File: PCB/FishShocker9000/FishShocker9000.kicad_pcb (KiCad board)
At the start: 2 copper layers, 133 parts, among them J1 Barrel_Jack, J10 P70-1000045R, J11 P70-1000045R, J12 P70-1000045R, J13 P70-1000045R, J14 P70-1000045R, J15 P70-1000045R, J16 P70-1000045R, J17 P70-1000045R, J18 P70-1000045R, J19 P70-1000045R, J20 P70-1000045R, J21 P70-1000045R, J22 P70-1000045R, J23 P70-1000045R, J24 P70-1000045R, J25 P70-1000045R, J26 P70-1000045R, J27 P70-1000045R, J28 P70-1000045R, J29 P70-1000045R, J3 P70-1000045R, J30 P70-1000045R, J31 P70-1000045R, J32 P70-1000045R, J33 P70-1000045R, J34 P70-1000045R, J35 P70-1000045R, J36 P70-1000045R, J37 P70-1000045R, J38 P70-1000045R, J39 P70-1000045R, J4 P70-1000045R, J40 P70-1000045R, J41 P70-1000045R, J42 P70-1000045R, J43 P70-1000045R, J44 P70-1000045R, J45 P70-1000045R, J46 P70-1000045R, J47 P70-1000045R, J48 P70-1000045R, J49 P70-1000045R, J5 P70-1000045R, J50 P70-1000045R, J51 P70-1000045R, J52 P70-1000045R, J53 P70-1000045R, J54 P70-1000045R, J55 P70-1000045R, J56 P70-1000045R, J57 P70-1000045R, J58 P70-1000045R, J59 P70-1000045R, J6 P70-1000045R, J60 P70-1000045R, J61 P70-1000045R, J62 P70-1000045R, J63 P70-1000045R, J64 P70-1000045R, J65 P70-1000045R, J66 P70-1000045R, J67 P70-1000045R, J68 P70-1000045R, J69 P70-1000045R, J7 P70-1000045R, J70 P70-1000045R, J71 P70-1000045R, J72 P70-1000045R, J73 P70-1000045R, J74 P70-1000045R, J8 P70-1000045R, J9 P70-1000045R, Q1 IRLZ44N, Q2 FQP27P06, U16 MP2331HGTL-Z, U19 DAC5311xDCK, U20 OPA197xD, U23 SN754410NE, U24 SN754410NE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

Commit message: Rerouted PCB layout to actually fit and work. Need to connect Pogo Pins
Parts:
- C8: footprint Capacitor_SMD:C_0201_0603Metric -> Capacitor_SMD:C_0603_1608Metric
- moved U23 7.50 mm to (319.4, 154.7)
- moved U24 7.50 mm to (319.4, 141.6)
- moved U25 7.50 mm to (319.4, 128.0)
- moved U26 7.50 mm to (319.4, 114.4)
- moved U29 7.50 mm to (319.4, 100.9)
- moved U30 7.50 mm to (319.4, 87.3)
- moved H4 6.52 mm to (271.5, 82.0)
- moved H1 5.52 mm to (405.5, 82.0)
- moved D10 4.03 mm to (356.1, 117.0)
- moved D11 4.03 mm to (356.0, 154.5)
- moved D12 4.03 mm to (393.0, 130.0)
- moved D13 4.03 mm to (374.6, 117.0)
- moved D2 4.03 mm to (374.5, 154.2)
- moved D3 4.03 mm to (393.1, 154.5)
- moved D4 4.03 mm to (355.9, 143.0)
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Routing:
- net BUCK_VOUT: track 68.2 -> 310.2 mm, vias 1 -> 2
- net GND: track 112.4 -> 225.7 mm, vias 16 -> 15
- net (no net): track 49.1 -> 0.00 mm
- net A11: track 152.2 -> 135.5 mm
- net Plate 5.1: track 43.9 -> 58.5 mm, vias 0 -> 1
- net Plate 9.1: track 72.5 -> 86.5 mm, vias 0 -> 1
- net Plate 12.2: track 86.9 -> 100.8 mm, vias 0 -> 1
- net Plate 3.1: track 29.6 -> 43.4 mm, vias 0 -> 1
- net Plate 1.1: track 17.4 -> 30.6 mm, vias 0 -> 1
- net Plate 9.2: track 65.4 -> 76.3 mm, vias 0 -> 1
- net Plate 7.1: track 61.2 -> 72.0 mm, vias 0 -> 1
- net Plate 5.2: track 36.8 -> 47.5 mm, vias 0 -> 1
- net Plate 12.1: track 79.8 -> 90.5 mm, vias 0 -> 1
- net Plate 3.2: track 22.5 -> 33.0 mm, vias 0 -> 1
- net Polarity Enable 2: track 214.9 -> 205.2 mm
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- added copper zone on B.Cu, net GND
- removed copper zone on F.Cu, net BUCK_VOUT
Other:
- board outline added: 140 x 285.9 mm
- board text removed: "LED ON = GOOD POWER"

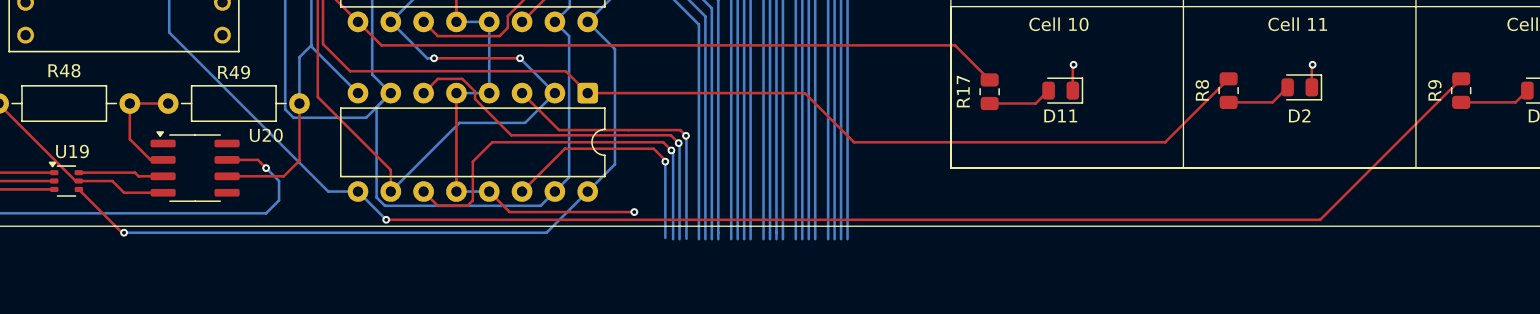
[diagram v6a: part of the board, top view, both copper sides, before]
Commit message: Fixed some other issues. Pogo Pins still not connected
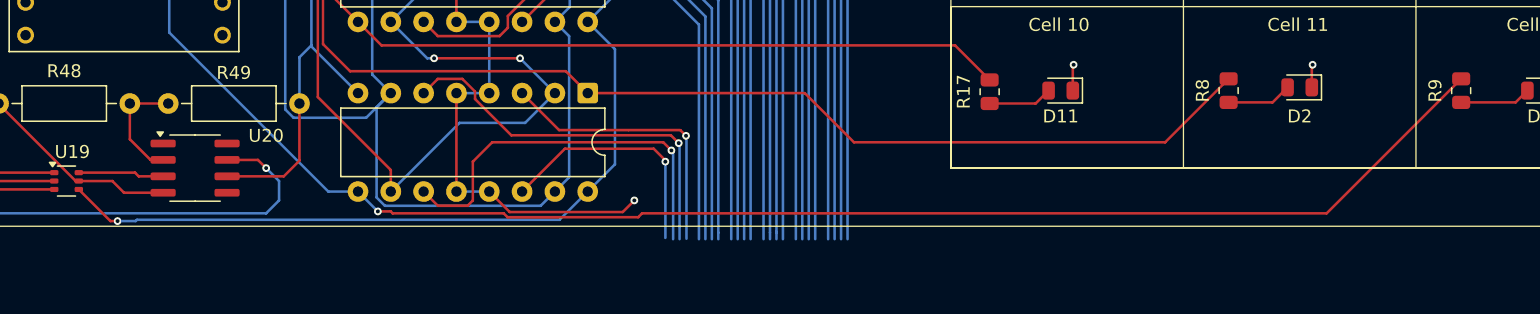
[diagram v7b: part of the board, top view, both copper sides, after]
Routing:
- net BUCK_VOUT: track 310.2 -> 309.4 mm
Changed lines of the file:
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@@
 	)
 	(segment
+		(start 282.45 164.6)
+		(end 280 162.15)
+		(width 0.2)
+		(layer "F.Cu")
+		(net 5)
+	)
+	(segment
 		(start 392.8625 96.8625)
 		(end 392 96)
@@
 	)
 	(segment
-		(start 283.5 165.5)
-		(end 283.35 165.5)
-		(width 0.2)
-		(layer "F.Cu")
-		(net 5)
-	)
-	(segment
 		(start 390.608198 107.5)
 		(end 388.5241 107.5)
@@
 	)
 	(segment
-		(start 387.0241 106)
-		(end 381.08294 106)
+		(start 283 164.6)
+		(end 282.45 164.6)
 		(width 0.2)
 		(layer "F.Cu")
@@
 	)
 	(segment
-		(start 382.9641 100.325)
-		(end 382.9641 103.17)
+		(start 387.0241 106)
+		(end 381.08294 106)
 		(width 0.2)
 		(layer "F.Cu")
@@
 	)
 	(segment
-		(start 283.35 165.5)
-		(end 280 162.15)
+		(start 382.9641 100.325)
+		(end 382.9641 103.17)
 		(width 0.2)
 		(layer "F.Cu")
@@
 	)
 	(via
-		(at 283.5 165.5)
+		(at 283 164.6)
 		(size 0.6)
 		(drill 0.3)
@@
 	)
 	(segment
+		(start 284.4 164.6)
+		(end 284.5 164.5)
+		(width 0.2)
+		(layer "B.Cu")
+		(net 5)
+	)
+	(segment
 		(start 321.5 110.608)
 		(end 321.5 119.949)
@@
 	)
 	(segment
+		(start 284.5 164.5)
+		(end 317.205 164.5)
+		(width 0.2)
+		(layer "B.Cu")
+		(net 5)
+	)
+	(segment
 		(start 285.28 91.79)
 		(end 278.93 98.14)
@@
 	)
 	(segment
+		(start 317.205 164.5)
+		(end 319.39 162.315)
+		(width 0.2)
+		(layer "B.Cu")
+		(net 5)
+	)
+	(segment
 		(start 319.39 162.315)
 		(end 321.5 160.205)
@@
 	)
 	(segment
-		(start 297.509 85.401)
-		(end 291.12 91.79)
+		(start 283 164.6)
+		(end 284.4 164.6)
 		(width 0.2)
 		(layer "B.Cu")
@@
 	)
 	(segment
-		(start 316.205 165.5)
-		(end 283.5 165.5)
+		(start 297.509 85.401)
+		(end 291.12 91.79)
 		(width 0.2)
 		(layer "B.Cu")
@@
 	)
 	(segment
-		(start 319.39 162.315)
-		(end 316.205 165.5)
-		(width 0.2)
-		(layer "B.Cu")
-		(net 5)
-	)
-	(segment
 		(start 321.5 147.071)
 		(end 319.39 149.181)
@@
 	)
 	(segment
-		(start 303.795 164.5)
-		(end 376.0875 164.5)
+		(start 304.1475 163.8525)
+		(end 304.295 164)
+		(width 0.2)
+		(layer "F.Cu")
+		(net 34)
+	)
+	(segment
+		(start 313.1889 164.301)
+		(end 323.3 164.301)
+		(width 0.2)
+		(layer "F.Cu")
+		(net 34)
+	)
+	(segment
+		(start 312.8879 164)
+		(end 313.1889 164.301)
+		(width 0.2)
+		(layer "F.Cu")
+		(net 34)
+	)
+	(segment
+		(start 323.601 164)
+		(end 376.5875 164)
+		(width 0.2)
+		(layer "F.Cu")
+		(net 34)
+	)
+	(segment
+		(start 304.295 164)
+		(end 312.8879 164)
 		(width 0.2)
 		(layer "F.Cu")
@@
 	)
 	(segment
-		(start 376.0875 164.5)
+		(start 376.5875 164)
 		(end 387 153.5875)
 		(width 0.2)
@@
 		(net 34)
 	)
+	(segment
+		(start 303.1475 163.8525)
+		(end 304.1475 163.8525)
+		(width 0.2)
+		(layer "F.Cu")
+		(net 34)
+	)
+	(segment
+		(start 323.3 164.301)
+		(end 323.601 164)
+		(width 0.2)
+		(layer "F.Cu")
+		(net 34)
+	)
 	(via
-		(at 303.795 164.5)
+		(at 303.1475 163.8525)
 		(size 0.6)
 		(drill 0.3)
@@
 	(segment
 		(start 301.61 162.315)
-		(end 303.795 164.5)
+		(end 303.1475 163.8525)
 		(width 0.2)
 		(layer "B.Cu")
@@
 	)
 	(segment
+		(start 313.355 163.9)
+		(end 311.77 162.315)
+		(width 0.2)
+		(layer "F.Cu")
+		(net 110)
+	)
+	(segment
 		(start 381.1 92.2)
 		(end 382.0841 92.2)
@@
 	)
 	(segment
+		(start 322.1 163.9)
+		(end 313.355 163.9)
+		(width 0.2)
+		(layer "F.Cu")
+		(net 110)
+	)
+	(segment
 		(start 309.23 141.561)
 		(end 309.23 149.181)
@@
 	)
 	(segment
-		(start 313.355 163.9)
-		(end 323 163.9)
+		(start 356.875 143)
+		(end 356.875 141.125)
 		(width 0.2)
 		(layer "F.Cu")
@@
 	)
 	(segment
-		(start 356.875 143)
-		(end 356.875 141.125)
+		(start 273.79 155.5)
+		(end 273.79 155.53487)
 		(width 0.2)
 		(layer "F.Cu")
@@
 	)
 	(segment
-		(start 273.79 155.5)
-		(end 273.79 155.53487)
+		(start 323 163)
+		(end 322.1 163.9)
 		(width 0.2)
 		(layer "F.Cu")
@@
 		(net 110)
 	)
-	(segment
-		(start 311.77 162.315)
-		(end 313.355 163.9)
-		(width 0.2)
-		(layer "F.Cu")
-		(net 110)
-	)
 	(via
 		(at 357 128)
@@
 	)
 	(via
-		(at 323 163.9)
+		(at 323 163)
 		(size 0.6)
 		(drill 0.3)

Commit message: Placed Pogo Pins
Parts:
- added J100: P70-1000045R, Library:HARWIN_P70-1000045R, F.Cu at (293.8, 347.6)
- added J101: P70-1000045R, Library:HARWIN_P70-1000045R, F.Cu at (309.7, 353.6)
- added J102: P70-1000045R, Library:HARWIN_P70-1000045R, F.Cu at (318.0, 250.9)
- added J103: P70-1000045R, Library:HARWIN_P70-1000045R, F.Cu at (310.1, 237.2)
- added J104: P70-1000045R, Library:HARWIN_P70-1000045R, F.Cu at (329.4, 286.1)
- added J105: P70-1000045R, Library:HARWIN_P70-1000045R, F.Cu at (345.3, 292.1)
- added J106: P70-1000045R, Library:HARWIN_P70-1000045R, F.Cu at (364.2, 278.3)
- added J107: P70-1000045R, Library:HARWIN_P70-1000045R, F.Cu at (380.6, 312.4)
- added J108: P70-1000045R, Library:HARWIN_P70-1000045R, F.Cu at (323.0, 329.9)
- added J109: P70-1000045R, Library:HARWIN_P70-1000045R, F.Cu at (309.7, 347.4)
- added J110: P70-1000045R, Library:HARWIN_P70-1000045R, F.Cu at (293.8, 224.7)
- added J111: P70-1000045R, Library:HARWIN_P70-1000045R, F.Cu at (285.3, 209.9)
- added J112: P70-1000045R, Library:HARWIN_P70-1000045R, F.Cu at (323.6, 213.8)
- added J113: P70-1000045R, Library:HARWIN_P70-1000045R, F.Cu at (315.9, 227.4)
- added J114: P70-1000045R, Library:HARWIN_P70-1000045R, F.Cu at (364.6, 271.2)
- added J115: P70-1000045R, Library:HARWIN_P70-1000045R, F.Cu at (381.5, 237.2)
- added J116: P70-1000045R, Library:HARWIN_P70-1000045R, F.Cu at (288.3, 275.3)
- added J117: P70-1000045R, Library:HARWIN_P70-1000045R, F.Cu at (285.3, 291.9)
- added J118: P70-1000045R, Library:HARWIN_P70-1000045R, F.Cu at (323.7, 295.8)
- added J119: P70-1000045R, Library:HARWIN_P70-1000045R, F.Cu at (345.7, 298.7)
- added J120: P70-1000045R, Library:HARWIN_P70-1000045R, F.Cu at (364.5, 319.2)
- added J121: P70-1000045R, Library:HARWIN_P70-1000045R, F.Cu at (381.3, 319.2)
- added J122: P70-1000045R, Library:HARWIN_P70-1000045R, F.Cu at (288.1, 193.3)
- added J123: P70-1000045R, Library:HARWIN_P70-1000045R, F.Cu at (280.4, 207.0)
- added J124: P70-1000045R, Library:HARWIN_P70-1000045R, F.Cu at (329.2, 244.9)
- added J125: P70-1000045R, Library:HARWIN_P70-1000045R, F.Cu at (345.2, 251.0)
- added J126: P70-1000045R, Library:HARWIN_P70-1000045R, F.Cu at (364.0, 237.1)
- added J127: P70-1000045R, Library:HARWIN_P70-1000045R, F.Cu at (356.5, 250.8)
- added J128: P70-1000045R, Library:HARWIN_P70-1000045R, F.Cu at (293.9, 312.5)
- added J129: P70-1000045R, Library:HARWIN_P70-1000045R, F.Cu at (309.7, 312.0)
- added J130: P70-1000045R, Library:HARWIN_P70-1000045R, F.Cu at (328.8, 298.8)
- added J131: P70-1000045R, Library:HARWIN_P70-1000045R, F.Cu at (315.8, 309.5)
- added J132: P70-1000045R, Library:HARWIN_P70-1000045R, F.Cu at (389.0, 333.0)
- added J133: P70-1000045R, Library:HARWIN_P70-1000045R, F.Cu at (351.3, 330.0)
- added J134: P70-1000045R, Library:HARWIN_P70-1000045R, F.Cu at (323.0, 207.1)
- added J135: P70-1000045R, Library:HARWIN_P70-1000045R, F.Cu at (309.8, 230.5)
- added J136: P70-1000045R, Library:HARWIN_P70-1000045R, F.Cu at (353.6, 230.3)
- added J137: P70-1000045R, Library:HARWIN_P70-1000045R, F.Cu at (345.1, 245.1)
- added J138: P70-1000045R, Library:HARWIN_P70-1000045R, F.Cu at (359.2, 234.5)
- added J139: P70-1000045R, Library:HARWIN_P70-1000045R, F.Cu at (351.4, 247.9)
- added J140: P70-1000045R, Library:HARWIN_P70-1000045R, F.Cu at (318.0, 291.9)
- added J141: P70-1000045R, Library:HARWIN_P70-1000045R, F.Cu at (310.2, 278.1)
- added J142: P70-1000045R, Library:HARWIN_P70-1000045R, F.Cu at (353.5, 312.3)
- added J143: P70-1000045R, Library:HARWIN_P70-1000045R, F.Cu at (320.9, 312.4)
- added J144: P70-1000045R, Library:HARWIN_P70-1000045R, F.Cu at (359.1, 316.2)
- added J145: P70-1000045R, Library:HARWIN_P70-1000045R, F.Cu at (356.4, 332.6)
- added J2: P70-1000045R, Library:HARWIN_P70-1000045R, F.Cu at (323.7, 172.9)
- added J75: P70-1000045R, Library:HARWIN_P70-1000045R, F.Cu at (316.0, 186.4)
- added J76: P70-1000045R, Library:HARWIN_P70-1000045R, F.Cu at (329.3, 204.0)
- added J77: P70-1000045R, Library:HARWIN_P70-1000045R, F.Cu at (320.8, 189.2)
- added J78: P70-1000045R, Library:HARWIN_P70-1000045R, F.Cu at (329.2, 210.0)
- added J79: P70-1000045R, Library:HARWIN_P70-1000045R, F.Cu at (345.1, 204.0)
- added J80: P70-1000045R, Library:HARWIN_P70-1000045R, F.Cu at (389.0, 210.0)
- added J81: P70-1000045R, Library:HARWIN_P70-1000045R, F.Cu at (380.6, 224.5)
- added J82: P70-1000045R, Library:HARWIN_P70-1000045R, F.Cu at (364.3, 196.3)
- added J83: P70-1000045R, Library:HARWIN_P70-1000045R, F.Cu at (386.3, 193.3)
- added J84: P70-1000045R, Library:HARWIN_P70-1000045R, F.Cu at (364.7, 224.4)
- added J85: P70-1000045R, Library:HARWIN_P70-1000045R, F.Cu at (380.6, 230.4)
- added J86: P70-1000045R, Library:HARWIN_P70-1000045R, F.Cu at (288.1, 234.2)
- added J87: P70-1000045R, Library:HARWIN_P70-1000045R, F.Cu at (280.2, 248.0)
- added J88: P70-1000045R, Library:HARWIN_P70-1000045R, F.Cu at (329.2, 292.0)
- added J89: P70-1000045R, Library:HARWIN_P70-1000045R, F.Cu at (345.2, 286.0)
- added J90: P70-1000045R, Library:HARWIN_P70-1000045R, F.Cu at (389.0, 291.8)
- added J91: P70-1000045R, Library:HARWIN_P70-1000045R, F.Cu at (351.4, 288.9)
- added J92: P70-1000045R, Library:HARWIN_P70-1000045R, F.Cu at (293.8, 353.4)
- added J93: P70-1000045R, Library:HARWIN_P70-1000045R, F.Cu at (315.2, 316.3)
- added J94: P70-1000045R, Library:HARWIN_P70-1000045R, F.Cu at (293.3, 237.3)
- added J95: P70-1000045R, Library:HARWIN_P70-1000045R, F.Cu at (285.4, 250.8)
- added J96: P70-1000045R, Library:HARWIN_P70-1000045R, F.Cu at (353.6, 271.4)
- added J97: P70-1000045R, Library:HARWIN_P70-1000045R, F.Cu at (350.8, 254.6)
- added J98: P70-1000045R, Library:HARWIN_P70-1000045R, F.Cu at (359.1, 275.3)
- added J99: P70-1000045R, Library:HARWIN_P70-1000045R, F.Cu at (356.3, 291.8)
- moved J54 122.0 mm to (285.4, 332.9)
- moved J65 117.4 mm to (364.8, 353.4)
- moved J74 116.0 mm to (380.6, 353.4)
- moved J69 115.6 mm to (394.0, 329.9)
- moved J61 114.6 mm to (318.1, 332.9)
- moved J68 114.6 mm to (345.1, 332.9)
- moved J67 114.5 mm to (329.3, 327.0)
- moved J66 111.4 mm to (380.8, 347.4)
- moved J73 111.1 mm to (364.8, 347.5)
- moved J58 109.6 mm to (280.2, 330.0)
- moved J53 109.6 mm to (293.2, 319.3)
- moved J71 105.6 mm to (329.3, 333.0)
- moved J62 100.7 mm to (310.2, 319.3)
- moved J59 99.1 mm to (364.9, 312.4)
- moved J57 96.9 mm to (288.1, 316.3)
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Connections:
- net A0 renamed CELL_1
- net A1 renamed CELL_2
- net A10 renamed CELL_11
- net A11 renamed CELL_12
- net A2 renamed CELL_3
- net A3 renamed CELL_4
- net A4 renamed CELL_5
- net A5 renamed CELL_6
- net A6 renamed CELL_7
- net A7 renamed CELL_8
- net A8 renamed CELL_9
- net A9 renamed CELL_10
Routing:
- net Plate 3.1: track 43.4 -> 201.4 mm, vias 1 -> 2
- net Plate 2.1: track 22.0 -> 167.5 mm, vias 1 -> 2
- net Plate 3.2: track 33.0 -> 161.6 mm, vias 1 -> 2
- net Plate 1.1: track 30.6 -> 155.1 mm, vias 1 -> 2
- net Plate 2.2: track 30.1 -> 151.2 mm, vias 1 -> 2
- net Plate 1.2: track 18.8 -> 97.6 mm, vias 1 -> 2
